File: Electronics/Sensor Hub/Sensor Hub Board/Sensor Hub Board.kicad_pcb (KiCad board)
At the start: 2 copper layers, 121 parts, among them IC202 TPS563202DRLR, IC203 TPS563202DRLR, IC302 STM32H723ZGT6, IC303 TJA1057GT/3, J202 Conn_01x02_Pin, J203 Conn_01x02_Pin, J204 Conn_01x02_Pin, J205 Conn_01x02_Pin, J206 Conn_01x02_Pin, J207 Screw_Terminal_01x02, J208 Conn_01x02_Pin, J209 Conn_01x02_Pin, J301 TC2030, J303 TYPE-C-31-M-12, J304 Screw_Terminal_01x03, J401 Conn_01x06_Pin, J402 Conn_01x06_Pin, J403 Conn_01x06_Pin, J404 Conn_01x06_Pin, J405 Conn_01x06_Pin, J406 Conn_01x06_Pin, J407 Conn_01x06_Pin, J408 Conn_01x06_Pin, J409 Conn_01x06_Pin, J410 Conn_01x06_Pin, J411 Conn_01x06_Pin, J412 Conn_01x06_Pin, J413 Conn_01x06_Pin, J414 Conn_01x06_Pin, J415 Conn_01x06_Pin, J416 Conn_01x06_Pin, Q201 DMP3028LFDE, SW301 SW_DIP_x02, U301 USBLC6-4SC6-ES, U302 USBLC6-4SC6-ES, U401 TCA9548APWR, U402 BMI270, U403 TCA9548APWR, U404 LIS3MDL, X301 25MHz_Clock, X302 32.768kHz_Clock

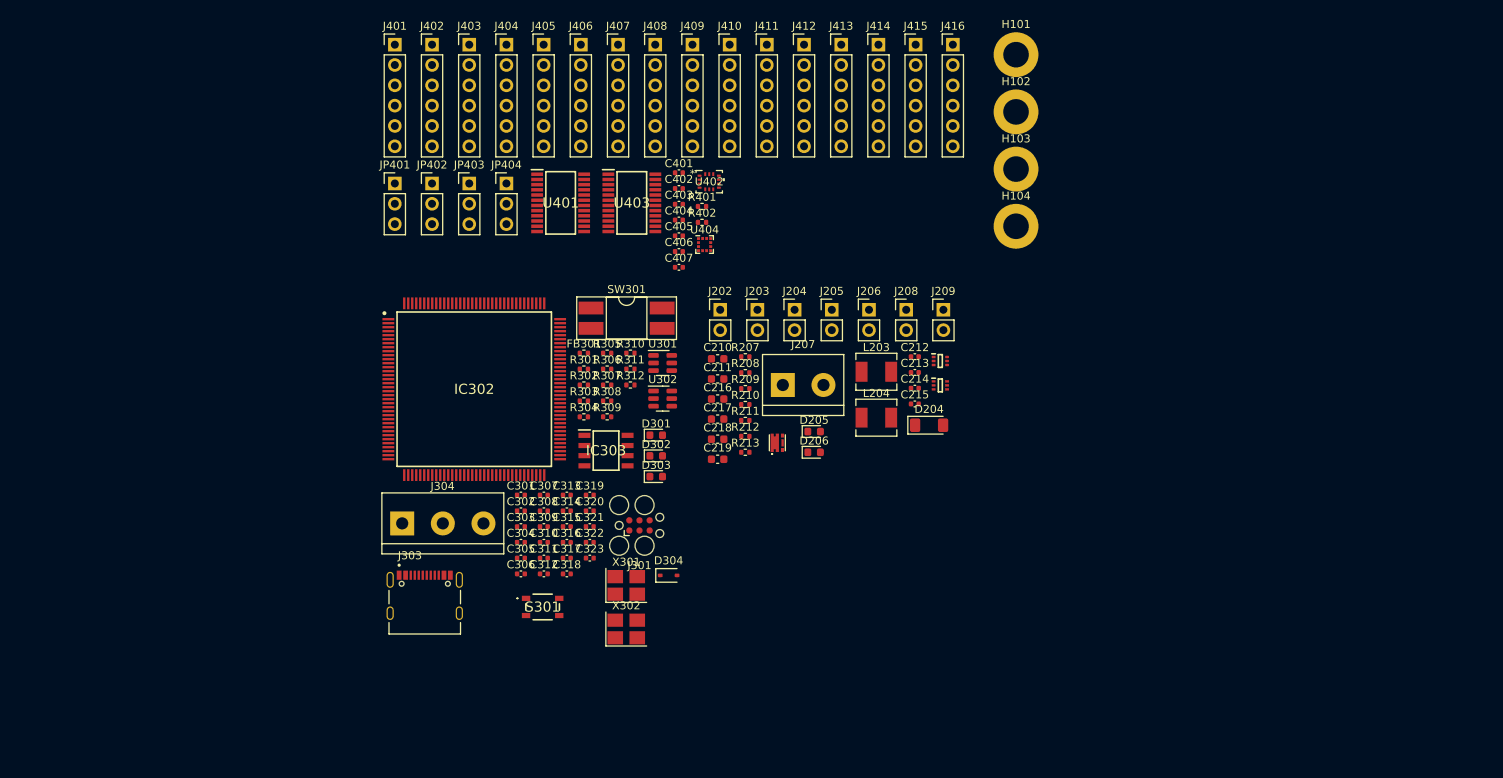
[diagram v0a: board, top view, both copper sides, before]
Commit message: PCB layout progress, spice simulations for power board
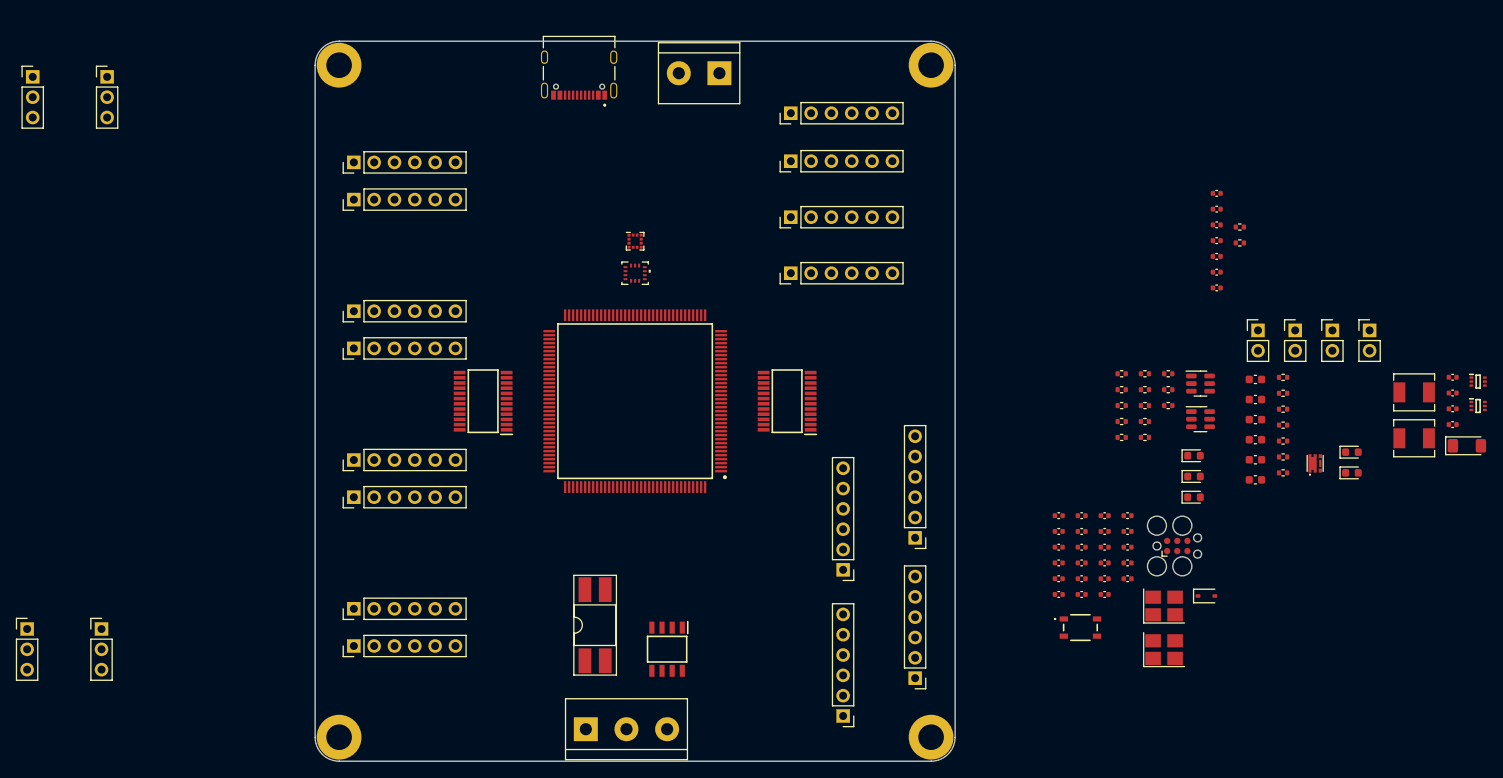
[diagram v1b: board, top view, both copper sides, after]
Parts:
- removed J206, J208, J209: Conn_01x02_Pin, Connector_PinHeader_2.54mm:PinHeader_1x02_P2.54mm_Vertical
- removed J304: Screw_Terminal_01x03, TerminalBlock:TerminalBlock_bornier-3_P5.08mm
- added J302: Screw_Terminal_01x03, TerminalBlock:TerminalBlock_bornier-3_P5.08mm, F.Cu at (133.8, 141.0)
- moved H102 115.2 mm to (103.0, 142.0)
- moved J401 100.9 mm to (166.0, 139.3), turned to 180 degrees
- moved J402 99.6 mm to (175.0, 134.6), turned to 180 degrees
- moved H101 84.6 mm to (103.0, 58.0)
- moved J403 76.5 mm to (104.8, 130.6), turned to 90 degrees
- moved J416 76.3 mm to (104.8, 70.2), turned to 90 degrees
- moved J405 75.6 mm to (166.0, 121.1), turned to 180 degrees
- moved J406 74.5 mm to (175.0, 117.1), turned to 180 degrees
- moved J404 73.0 mm to (104.8, 126.0), turned to 90 degrees
- moved J415 72.8 mm to (104.8, 74.8), turned to 90 degrees
- moved JP401 72.2 mm to (64.0, 128.5)
- moved JP403 72.2 mm to (73.3, 128.5)
- moved J303 72.1 mm to (133.0, 57.0), turned to 180 degrees
- moved D301 67.3 mm to (209.9, 106.8)
- moved D302 67.3 mm to (209.9, 109.4)
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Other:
- board outline added: 80 x 90 mm

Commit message: Gateway board layout complete and routing begun
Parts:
- removed J205: Conn_01x02_Pin, Connector_PinHeader_2.54mm:PinHeader_1x02_P2.54mm_Vertical
- removed U301: USBLC6-4SC6-ES, Package_TO_SOT_SMD:SOT-23-6
- added J201: JST-XH-2.50mm, Connector_JST:JST_XH_B2B-XH-A_1x02_P2.50mm_Vertical, F.Cu at (230.5, 80.0)
- J202, J203, J204: value Conn_01x02_Pin -> JST-XH-2.50mm; footprint Connector_PinHeader_2.54mm:PinHeader_1x02_P2.54mm_Vertical -> Connector_JST:JST_XH_B2B-XH-A_1x02_P2.50mm_Vertical
- J207: value Screw_Terminal_01x02 -> Pluggable_Terminal_01x02; footprint TerminalBlock:TerminalBlock_bornier-2_P5.08mm -> MSL Footprints:Pluggable_terminal-2_P5.08mm
- J302: value Screw_Terminal_01x03 -> Pluggable_Terminal_01x03; footprint TerminalBlock:TerminalBlock_bornier-3_P5.08mm -> MSL Footprints:Pluggable_terminal-3_P5.08mm
- R207: value 330R -> 4k7
- moved J207 79.2 mm to (145.5, 138.0), turned to 0 degrees
- moved IC303 15.8 mm to (135.0, 118.0)
- moved J302 6.64 mm to (127.9, 138.0)
- moved SW301 2.00 mm to (135.0, 126.0), turned to 180 degrees
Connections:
- J202 pad 1: +5V -> +3V3
- J302 pad 1: /Microcontroller/CANL -> /Microcontroller/CANH
- J302 pad 3: /Microcontroller/CANH -> /Microcontroller/CANL
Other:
- copper layers 2 -> 4

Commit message: Sensor hub board done
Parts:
- removed C211, C216, C217, C218, C219: 22u, Capacitor_SMD:C_0603_1608Metric
- removed C212, C213, C214, C215: 100n, Capacitor_SMD:C_0402_1005Metric
- removed D204: ZMM10V, Diode_SMD:D_MiniMELF
- removed D205, D206: GREEN, LED_SMD:LED_0603_1608Metric
- removed IC203: TPS563202DRLR, MSL Footprints:SOTFL50P160X60-6N
- removed IC303: TJA1057GT/3, MSL Footprints:SOIC127P600X175-8N
- removed J201, J202, J204: JST-XH-2.50mm, Connector_JST:JST_XH_B2B-XH-A_1x02_P2.50mm_Vertical
- removed J207: Pluggable_Terminal_01x02, MSL Footprints:Pluggable_terminal-2_P5.08mm
- removed L203: 4u7, Inductor_SMD:L_Chilisin_BMRA00040420
- removed L204: 3u3, Inductor_SMD:L_Chilisin_BMRA00040420
- removed R208: 52k, Resistor_SMD:R_0402_1005Metric
- removed R209, R211: 10k, Resistor_SMD:R_0402_1005Metric
- removed R210: 31k, Resistor_SMD:R_0402_1005Metric
- removed R212: 2k2, Resistor_SMD:R_0402_1005Metric
- removed R213: 1k5, Resistor_SMD:R_0402_1005Metric
- added C201: 22u, Capacitor_SMD:C_0603_1608Metric, F.Cu at (154.0, 122.0)
- added C202: 22u, Capacitor_SMD:C_0603_1608Metric, F.Cu at (126.0, 122.0)
- added C203: 100n, Capacitor_SMD:C_0402_1005Metric, F.Cu at (152.8, 122.0)
- added C204: 100n, Capacitor_SMD:C_0402_1005Metric, F.Cu at (127.2, 121.7)
- added C205: 100n, Capacitor_SMD:C_0402_1005Metric, F.Cu at (148.8, 124.3)
- added C206: 100n, Capacitor_SMD:C_0402_1005Metric, F.Cu at (127.0, 124.0)
- added C207: 22u, Capacitor_SMD:C_0603_1608Metric, F.Cu at (148.3, 121.1)
- added C208: 22u, Capacitor_SMD:C_0603_1608Metric, F.Cu at (131.7, 122.8)
- added C209: 22u, Capacitor_SMD:C_0603_1608Metric, F.Cu at (148.3, 122.7)
- added C324: 10n, Capacitor_SMD:C_0402_1005Metric, F.Cu at (145.0, 65.3)
- added D201: ZMM10V, Diode_SMD:D_MiniMELF, F.Cu at (131.5, 127.5)
- added D202: GREEN, LED_SMD:LED_0603_1608Metric, F.Cu at (145.7, 119.5)
- added D203: GREEN, LED_SMD:LED_0603_1608Metric, F.Cu at (134.6, 119.5)
- added G***: LOGO, MSL Footprints:ICRS_20mm, F.Cu at (140.0, 91.0)
- added G***: LOGO, footprints:ICRS Medium, B.Cu at (140.0, 100.5)
- added G***: LOGO, MSL Footprints:DC_logo_4mm, B.Cu at (136.2, 142.0)
- added IC201: TPS563202DRLR, MSL Footprints:SOTFL50P160X60-6N, F.Cu at (151.0, 122.0)
- added IC301: TJA1057GT/3, MSL Footprints:SOIC127P600X175-8N, F.Cu at (150.8, 110.0)
- added J304: JST_SH_1mm_1x4, MSL Footprints:JST_SH_1mm_1x4, F.Cu at (150.8, 60.2)
- added L201: 4u7, Inductor_SMD:L_Chilisin_BMRA00040420, F.Cu at (151.0, 118.0)
- added L202: 3u3, Inductor_SMD:L_Chilisin_BMRA00040420, F.Cu at (129.0, 118.0)
- added R201: 4k7, Resistor_SMD:R_0402_1005Metric, F.Cu at (140.0, 130.0)
- added R202: 52k, Resistor_SMD:R_0402_1005Metric, F.Cu at (151.3, 124.0)
- added R203: 10k, Resistor_SMD:R_0402_1005Metric, F.Cu at (153.3, 124.0)
- added R204: 31k, Resistor_SMD:R_0402_1005Metric, F.Cu at (131.0, 124.0)
- added R205: 10k, Resistor_SMD:R_0402_1005Metric, F.Cu at (129.0, 124.0)
- added R206: 2k2, Resistor_SMD:R_0402_1005Metric, F.Cu at (145.7, 120.8)
- added R313: 10k, Resistor_SMD:R_0402_1005Metric, F.Cu at (143.0, 65.3)
- added R314: 2k2, Resistor_SMD:R_0402_1005Metric, F.Cu at (154.0, 92.0)
- added R315: 2k2, Resistor_SMD:R_0402_1005Metric, F.Cu at (154.0, 90.0)
- added S302: TS20-42-25-WT-160-SMT-TR, MSL Footprints:TS204225WT160SMTTRMSL, F.Cu at (144.0, 58.5)
- C402: value 1u -> 100n
- C406: value 100n -> 1u
- J203: value JST-XH-2.50mm -> Pluggable_Terminal_01x02; footprint Connector_JST:JST_XH_B2B-XH-A_1x02_P2.50mm_Vertical -> MSL Footprints:Pluggable_terminal-2_P5.08mm
- J301: footprint Connector:Tag-Connect_TC2030-IDC-FP_2x03_P1.27mm_Vertical -> MSL Footprints:Tag-Connect_TC2030-IDC-FP_2x03_P1.27mm_Vertical
- J401, J402, J403, J404, J405, J406, J407, J408, J409, J410, J411, J412, J413, J414, J415, J416: value Conn_01x06_Pin -> JST_2.5mm_1x6; footprint Connector_PinHeader_2.54mm:PinHeader_1x06_P2.54mm_Vertical -> Connector_JST:JST_XH_B6B-XH-A_1x06_P2.50mm_Vertical
- R207: value 4k7 -> 1k5
- moved IC202 118.9 mm to (129.0, 122.0), turned to -90 degrees
- moved J203 104.7 mm to (128.9, 138.0)
- moved D304 103.9 mm to (126.4, 64.6), turned to 90 degrees
- moved JP403 99.0 mm to (152.0, 68.5)
- moved Q201 96.3 mm to (131.8, 132.1), turned to 90 degrees
- moved C404 96.0 mm to (120.0, 104.8)
- moved JP402 92.2 mm to (128.0, 126.5)
- moved R402 90.9 mm to (127.5, 102.8), turned to -90 degrees
- moved S301 89.9 mm to (139.0, 58.5), turned to 90 degrees
- moved R207 89.6 mm to (134.6, 120.8), turned to 180 degrees
- moved C210 89.1 mm to (131.7, 121.3), turned to 180 degrees
- moved C402 88.0 mm to (136.6, 120.2), turned to 90 degrees
- moved JP401 88.0 mm to (152.0, 126.5)
- moved U302 87.3 mm to (131.5, 65.5), turned to 90 degrees
- moved J301 86.4 mm to (134.6, 72.1), turned to 180 degrees
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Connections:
- C210 pad 1: VIN -> +3.3V
- C301 pad 1: +3V3 -> +3.3V
- C302 pad 2: +3V3 -> +3.3V
- C306 pad 1: +3V3 -> +3.3V
- C307 pad 1: /Microcontroller/VREF+ -> /Microcontroller/VDDA
- C308 pad 1: +3V3 -> +3.3V
- C309 pad 1: /Microcontroller/VREF+ -> /Microcontroller/VDDA
- C310 pad 1: +3V3 -> +3.3V
- C311 pad 1: +3V3 -> +3.3V
- C312 pad 1: +3V3 -> +3.3V
- C313 pad 1: +3V3 -> +3.3V
- C314 pad 1: +3V3 -> +3.3V
- C315 pad 1: +3V3 -> +3.3V
- C316 pad 1: +3V3 -> +3.3V
- C317 pad 1: +3V3 -> +3.3V
- C318 pad 1: +3V3 -> +3.3V
- C320 pad 1: +3V3 -> +3.3V
- C321 pad 1: +3V3 -> +3.3V
- C322 pad 1: +3V3 -> +3.3V
- C401 pad 1: +3V3 -> +3.3V
- C402 pad 1: +3V3 -> +3.3V
- C403 pad 1: +3V3 -> +3.3V
- C404 pad 1: +3V3 -> +3.3V
- C405 pad 1: /Sensors & connectors/MAG_C1 -> +3.3V
- C406 pad 1: +3V3 -> +3.3V
- C407 pad 1: +3V3 -> /Sensors & connectors/MAG_C1
- FB301 pad 1: /Microcontroller/VREF+ -> /Microcontroller/VDDA
- FB301 pad 2: +3V3 -> +3.3V
- IC202 pad 2: /Power/5V_SW -> /Power/3V3_SW
- IC202 pad 4: /Power/5V_BST -> /Power/3V3_BST
- IC202 pad 6: /Power/5V_FB -> /Power/3V3_FB
- IC302 pad 1: unconnected-(IC302-PE2-Pad1) -> MAG_SCK
- IC302 pad 10: SDA2_MCU -> GPIO9A
- IC302 pad 100: unconnected-(IC302-PA8-Pad100) -> SCL3_MCU
- IC302 pad 108: +3V3 -> +3.3V
- IC302 pad 11: SCL2_MCU -> GPIO8B
- IC302 pad 110: unconnected-(IC302-PA15-Pad110) -> GPIO15B
- IC302 pad 111: unconnected-(IC302-PC10-Pad111) -> GPIO15A
- IC302 pad 112: unconnected-(IC302-PC11-Pad112) -> GPIO14B
- IC302 pad 113: unconnected-(IC302-PC12-Pad113) -> GPIO14A
- IC302 pad 116: unconnected-(IC302-PD2-Pad116) -> GPIO13B
- IC302 pad 117: unconnected-(IC302-PD3-Pad117) -> GPIO13A
- IC302 pad 118: unconnected-(IC302-PD4-Pad118) -> GPIO12B
- IC302 pad 119: unconnected-(IC302-PD5-Pad119) -> GPIO12A
- IC302 pad 12: unconnected-(IC302-PF2-Pad12) -> GPIO8A
- IC302 pad 121: +3V3 -> +3.3V
- IC302 pad 131: +3V3 -> +3.3V
- IC302 pad 134: unconnected-(IC302-PB4-Pad134) -> GPIO11A
- IC302 pad 135: unconnected-(IC302-PB5-Pad135) -> GPIO10B
- IC302 pad 139: unconnected-(IC302-PB8-Pad139) -> MUX1_RST
- IC302 pad 141: unconnected-(IC302-PE0-Pad141) -> GPIO11B
- IC302 pad 142: unconnected-(IC302-PE1-Pad142) -> GPIO10A
- IC302 pad 143: +3V3 -> +3.3V
- IC302 pad 144: +3V3 -> +3.3V
- IC302 pad 17: +3V3 -> +3.3V
- IC302 pad 18: unconnected-(IC302-PF6-Pad18) -> IMU_CS
- IC302 pad 19: unconnected-(IC302-PF7-Pad19) -> IMU_SCK
- IC302 pad 2: unconnected-(IC302-PE3-Pad2) -> IMU_INT1
- IC302 pad 20: unconnected-(IC302-PF8-Pad20) -> IMU_MISO
- IC302 pad 21: unconnected-(IC302-PF9-Pad21) -> IMU_MOSI
- IC302 pad 26: unconnected-(IC302-PC0-Pad26) -> IMU_INT2
- IC302 pad 27: unconnected-(IC302-PC1-Pad27) -> MAG_DRDY
- IC302 pad 28: unconnected-(IC302-PC2_C-Pad28) -> MAG_INT
- IC302 pad 3: unconnected-(IC302-PE4-Pad3) -> MAG_CS
- IC302 pad 30: +3V3 -> +3.3V
- IC302 pad 33: /Microcontroller/VREF+ -> /Microcontroller/VDDA
- IC302 pad 34: unconnected-(IC302-PA0-Pad34) -> SILENT
- IC302 pad 36: unconnected-(IC302-PA2-Pad36) -> GPIO0B
- IC302 pad 37: unconnected-(IC302-PA3-Pad37) -> GPIO1A
- IC302 pad 39: +3V3 -> +3.3V
- IC302 pad 4: unconnected-(IC302-PE5-Pad4) -> MAG_MISO
- IC302 pad 40: IMU_CS -> GPIO0A
- IC302 pad 41: IMU_SCK -> GPIO1B
- IC302 pad 42: IMU_MISO -> GPIO3A
- IC302 pad 43: IMU_MOSI -> GPIO3B
- IC302 pad 44: unconnected-(IC302-PC4-Pad44) -> MUX2_RST
- IC302 pad 46: unconnected-(IC302-PB0-Pad46) -> GPIO7B
- IC302 pad 47: unconnected-(IC302-PB1-Pad47) -> GPIO7A
- IC302 pad 48: unconnected-(IC302-PB2-Pad48) -> GPIO6B
- IC302 pad 49: unconnected-(IC302-PF11-Pad49) -> GPIO6A
- IC302 pad 5: unconnected-(IC302-PE6-Pad5) -> MAG_MOSI
- IC302 pad 52: +3V3 -> +3.3V
- IC302 pad 54: unconnected-(IC302-PF14-Pad54) -> SCL4_MCU
- IC302 pad 55: unconnected-(IC302-PF15-Pad55) -> SDA4_MCU
- IC302 pad 6: +3V3 -> +3.3V
- IC302 pad 62: +3V3 -> +3.3V
- IC302 pad 64: unconnected-(IC302-PE11-Pad64) -> GPIO4A
- IC302 pad 65: unconnected-(IC302-PE12-Pad65) -> GPIO4B
- IC302 pad 66: unconnected-(IC302-PE13-Pad66) -> GPIO2A
- IC302 pad 67: unconnected-(IC302-PE14-Pad67) -> GPIO2B
- IC302 pad 69: unconnected-(IC302-PB10-Pad69) -> GPIO5A
- IC302 pad 7: unconnected-(IC302-PC13-Pad7) -> GPIO9B
- IC302 pad 70: unconnected-(IC302-PB11-Pad70) -> GPIO5B
- IC302 pad 72: +3V3 -> +3.3V
- IC302 pad 73: MAG_CS -> LEDG
- IC302 pad 74: MAG_SCK -> LEDR
- IC302 pad 75: MAG_MISO -> LEDB
- IC302 pad 76: MAG_MOSI -> unconnected-(IC302-PB15-Pad76)
- IC302 pad 84: +3V3 -> +3.3V
- IC302 pad 90: unconnected-(IC302-PG5-Pad90) -> BTN
- IC302 pad 95: +3V3 -> +3.3V
- IC302 pad 99: unconnected-(IC302-PC9-Pad99) -> SDA3_MCU
- J203 pad 1: +5V -> VIN_RAW
- J301 pad 1: +3V3 -> +3.3V
- J303 pad S2: unconnected-(J303-SHIELD-PadS1) -> unconnected-(J303-SHIELD-PadS2)
- J303 pad S3: unconnected-(J303-SHIELD-PadS1) -> unconnected-(J303-SHIELD-PadS3)
- J303 pad S4: unconnected-(J303-SHIELD-PadS1) -> unconnected-(J303-SHIELD-PadS4)
- J409 pad 6: GPIO0B -> GPIO4B
- JP401 pad 1: +3V3 -> +3.3V
- JP402 pad 1: +3V3 -> +3.3V
- JP403 pad 1: +3V3 -> +3.3V
- JP404 pad 1: +3V3 -> +3.3V
- Q201 pad 8: (no net) -> VIN_RAW
- R207 pad 1: /Power/RP_PMOS_G -> /Power/3V3_LED_K
- R304 pad 2: +3V3 -> +3.3V
- R309 pad 1: +3V3 -> +3.3V
- R310 pad 1: +3V3 -> +3.3V
- R311 pad 1: +3V3 -> +3.3V
- R311 pad 2: SCL2_MCU -> SCL3_MCU
- R312 pad 1: +3V3 -> +3.3V
- R312 pad 2: SDA2_MCU -> SDA3_MCU
- R401 pad 2: +3V3 -> +3.3V
- R402 pad 2: +3V3 -> +3.3V
- SW301 pad 2: +3V3 -> +3.3V
- U302 pad 1: /Microcontroller/CC1 -> /Microcontroller/CC2
- U302 pad 3: /Microcontroller/CC2 -> /Microcontroller/CC1
- U302 pad 4: USB_DP -> USB_DN
- U302 pad 6: USB_DN -> USB_DP
- U401 pad 10: SDA11 -> SDA5
- U401 pad 11: SCL11 -> SCL5
- U401 pad 13: SDA12 -> SDA7
- U401 pad 14: SCL12 -> SCL7
- U401 pad 15: SDA13 -> SDA6
- U401 pad 16: SCL13 -> SCL6
- U401 pad 17: SDA14 -> SDA0
- U401 pad 18: SCL14 -> SCL0
- U401 pad 19: SDA15 -> SDA1
- U401 pad 20: SCL15 -> SCL1
- U401 pad 22: SCL2_MCU -> SCL4_MCU
- U401 pad 23: SDA2_MCU -> SDA4_MCU
- U401 pad 24: +3V3 -> +3.3V
- U401 pad 4: SDA8 -> SDA2
- U401 pad 5: SCL8 -> SCL2
- U401 pad 6: SDA9 -> SDA3
- U401 pad 7: SCL9 -> SCL3
- U401 pad 8: SDA10 -> SDA4
- U401 pad 9: SCL10 -> SCL4
- U402 pad 5: +3V3 -> +3.3V
- U402 pad 8: +3V3 -> +3.3V
- U403 pad 10: SDA3 -> SDA13
- U403 pad 11: SCL3 -> SCL13
- U403 pad 13: SDA4 -> SDA14
- U403 pad 14: SCL4 -> SCL14
- U403 pad 15: SDA5 -> SDA12
- U403 pad 16: SCL5 -> SCL12
- U403 pad 17: SDA6 -> SDA11
- U403 pad 18: SCL6 -> SCL11
- U403 pad 19: SDA7 -> SDA10
- U403 pad 20: SCL7 -> SCL10
- U403 pad 24: +3V3 -> +3.3V
- U403 pad 4: SDA0 -> SDA9
- U403 pad 5: SCL0 -> SCL9
- U403 pad 6: SDA1 -> SDA8
- U403 pad 7: SCL1 -> SCL8
- U403 pad 8: SDA2 -> SDA15
- U403 pad 9: SCL2 -> SCL15
- U404 pad 5: +3V3 -> +3.3V
- U404 pad 6: +3V3 -> +3.3V
- X301 pad 4: +3V3 -> +3.3V
- X302 pad 4: +3V3 -> +3.3V
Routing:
- net GND: track 0.00 -> 91.4 mm, vias 0 -> 72
- net GPIO2B: track 0.00 -> 79.4 mm, vias 0 -> 4
- net +3.3V: track 0.00 -> 79.0 mm, vias 0 -> 44
- net GPIO2A: track 0.00 -> 74.2 mm, vias 0 -> 4
- net NRST: track 0.00 -> 64.6 mm, vias 0 -> 2
- net VDDIO2: track 0.00 -> 59.2 mm
- net VDDIO3: track 0.00 -> 58.3 mm
- net VDDIO1: track 0.00 -> 52.0 mm, vias 0 -> 3
- net VDDIO4: track 0.00 -> 49.9 mm
- net GPIO0A: track 0.00 -> 45.6 mm, vias 0 -> 4
- net GPIO0B: track 0.00 -> 45.0 mm, vias 0 -> 4
- net SDA15: track 0.00 -> 43.6 mm
- net SDA0: track 0.00 -> 42.9 mm
- net CAN_RX: track 0.00 -> 42.5 mm
- net GPIO11B: track 0.00 -> 42.0 mm, vias 0 -> 2
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- added copper zone on B.Cu, net +3.3V
- added copper zone on F.Cu, net +3.3V
- added copper zone on B.Cu, net +5V
- added copper zone on F.Cu, net +5V
- added copper zone on F.Cu, net /Power/3V3_SW
- added copper zone on F.Cu, net /Power/5V_SW
- added copper zone on F.Cu, net GND
- added copper zone on In1.Cu, net GND
- added copper zone on In2.Cu, net GND
- added copper zone on B.Cu, net VIN
- added copper zone on F.Cu, net VIN
- added copper zone on F.Cu, net VIN_RAW
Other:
- board size 80 x 90 mm -> 64 x 90 mm
- board text added: "GND"
- board text added: "IO"
- board text added: "SCL"
- board text added: "SDA"
- board text added: "VCC1"
- board text added: "locked"

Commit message: Motor driver and power boards done
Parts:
- added REF**: WEEE-Logo_5.6x8mm_SilkScreen, Symbol:WEEE-Logo_5.6x8mm_SilkScreen, B.Cu at (145.0, 124.2)
- added REF**: ESD-Logo_8.9x8mm_SilkScreen, Symbol:ESD-Logo_8.9x8mm_SilkScreen, B.Cu at (135.2, 124.2)
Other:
- board text added: "-Y"
- board text added: "Designed by Ben Smith 2023"
- board text added: "IMU Axis"
- board text added: "MAG Axis"
- board text added: "X"
- board text added: "Y"
- board text added: "Z"

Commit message: All boards done
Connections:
- H101 pad 1: GND -> unconnected-(H101-Pad1)
- H102 pad 1: GND -> unconnected-(H102-Pad1)
- H103 pad 1: GND -> unconnected-(H103-Pad1)
- H104 pad 1: GND -> unconnected-(H104-Pad1)
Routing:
- net +3.3V: track 79.0 -> 84.3 mm, vias 44 -> 43
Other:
- board text removed: "-Y"
- board text removed: "Designed by Ben Smith 2023"
- board text removed: "GND"
- board text removed: "IMU Axis"
- board text removed: "IO"
- board text removed: "MAG Axis"
- board text removed: "SCL"
- board text removed: "SDA"
- board text removed: "VCC1"
- board text removed: "X"
- board text removed: "Y"
- board text removed: "Z"
